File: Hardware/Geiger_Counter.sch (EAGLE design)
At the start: 55 parts, among them Q1 MPSA42, Q2 MPSA18, Q3 MMBT4403, Q4 MPSA18, U10 FT232RL-BASICSSOP, U17 AVR_SPI_PRG_6PTH, U7 TRANSFORMERAUDIO, X1 USBSMD

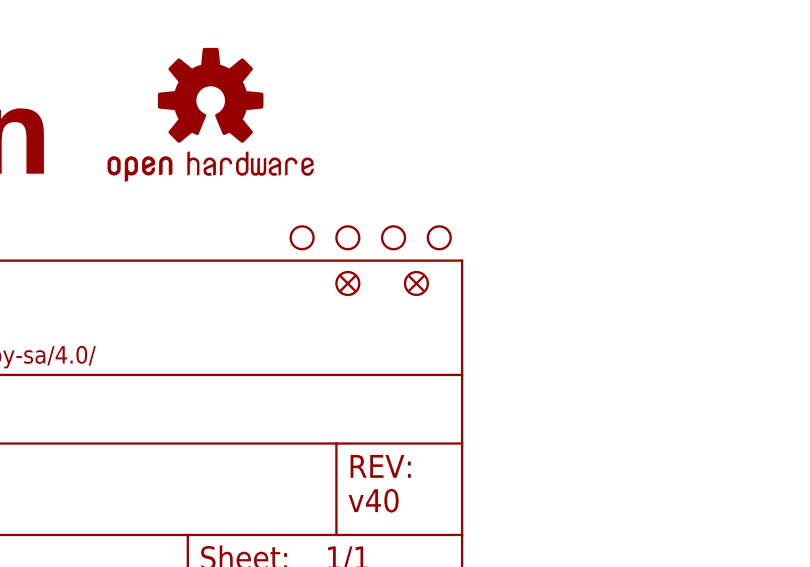
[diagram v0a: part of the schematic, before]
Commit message: added regular fiducial
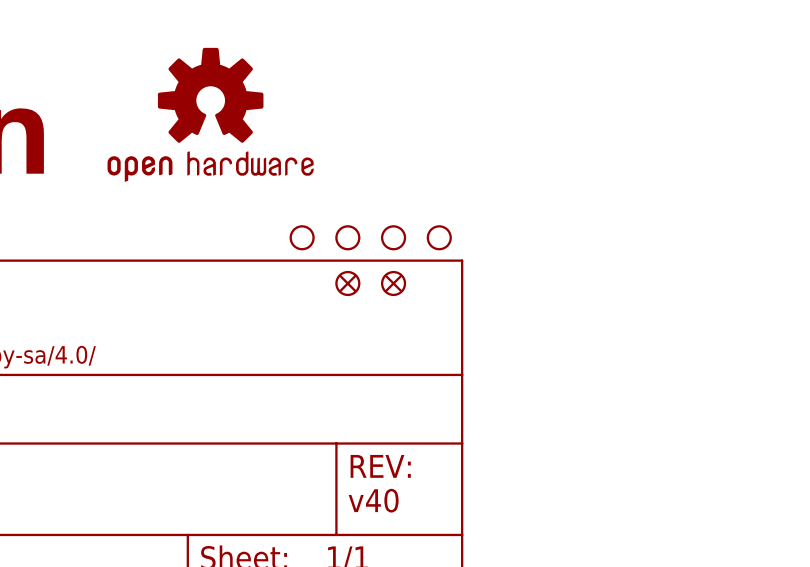
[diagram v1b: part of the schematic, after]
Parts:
- removed JP1, JP3: FIDUCIALUFIDUCIAL, SparkFun:FIDUCIALUFIDUCIAL
- added FID1, FID2: FIDUCIAL1X2, SparkFun-Aesthetics:FIDUCIAL1X2
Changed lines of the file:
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@@
 <?xml version="1.0" encoding="utf-8"?>
 <!DOCTYPE eagle SYSTEM "eagle.dtd">
-<eagle version="6.4">
+<eagle version="6.6.0">
 <drawing>
 <settings>
@@
 <part name="R9" library="SparkFun" deviceset="RESISTOR" device="AXIAL-0.3" value="10M"/>
 <part name="C1" library="SparkFun-Capacitors" deviceset="0.1UF-25V(+80/-20%)(0603)" device="" value="0.1uF"/>
-<part name="JP1" library="SparkFun" deviceset="FIDUCIAL" device="UFIDUCIAL"/>
-<part name="JP3" library="SparkFun" deviceset="FIDUCIAL" device="UFIDUCIAL"/>
 <part name="LOGO1" library="SparkFun-Aesthetics" deviceset="OSHW-LOGO" device="M"/>
 <part name="LOGO2" library="SparkFun-Aesthetics" deviceset="SFE_LOGO_NAME_FLAME" device=".1_INCH"/>
 <part name="GND2" library="SparkFun" deviceset="GND" device=""/>
+<part name="FID1" library="SparkFun-Aesthetics" deviceset="FIDUCIAL" device="1X2"/>
+<part name="FID2" library="SparkFun-Aesthetics" deviceset="FIDUCIAL" device="1X2"/>
 </parts>
 <sheets>
@@
 <instance part="LOGO1" gate="G$1" x="220.98" y="53.34"/>
 <instance part="LOGO2" gate="G$1" x="147.32" y="40.64"/>
-<instance part="JP1" gate="G$1" x="243.84" y="33.02"/>
-<instance part="JP3" gate="G$1" x="236.22" y="33.02"/>
 <instance part="GND2" gate="1" x="50.8" y="83.82"/>
+<instance part="FID1" gate="G$1" x="236.22" y="33.02"/>
+<instance part="FID2" gate="G$1" x="241.3" y="33.02"/>
 </instances>
 <busses>
